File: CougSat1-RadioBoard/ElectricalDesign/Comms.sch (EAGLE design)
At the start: 409 parts, among them J1 230mm Antenna, J2 CougSat Card, J3 700mm Antenna, J4 SWD, Q1 CSD25402Q3A, Q12 DMN53D0LDW, Q2 CSD25402Q3A, Q3 DMN53D0LDW, Q9 DMN53D0LDW, U1 INA199C1, U10 HMC452QS16G, U11 AD8515, U12 AD7291, U13 AD8515, U14 LP5907MFX-3.1, U15 AD9761, U16 TXS0102DQM, U18 TXS0102DQM, U19 MMZ09332B, U2 LP5907MFX-3.1, U20 ADF4360, U21 HMC545A, U22 AD9761, U23 MAAM-011229, U24 AD8515, U25 MAAM-011229, U26 AD8345, U28 AD8348, U29 AD7291, U3 TPS61236, U30 TXS0102DQM, U31 MAAM-011229, U32 AD8515, U35 TXS0102DQM, U36 ADF4360, U37 MAAM-011229, U39 AD8515, U4 AD8346, U40 AD8515, U42 TXS0102DQM, U43 INA199C2, U44 TXS0102DQM, U45 TXS0102DQM, U46 TXS0102DQM, U47 TXS0102DQM, U48 AD7291, U49 AD8515, U5 ADF4360, U50 INA199C2, U51 LP5907MFX-3.1, U52 INA199C2, U53 INA199C1, U54 TXS0102DQM, U55 TXS0102DQM, U6 STM32L496VGT, U7 GRF2133, U8 IS25LP016D, U9 IS25LP016D, Y1 19.68MHz ±2.5ppm, Y2 8MHz ±10ppm, Y3 32.768kHz ±10ppm, Y4 19.68MHz ±2.5ppm, Y5 19.68MHz ±2.5ppm

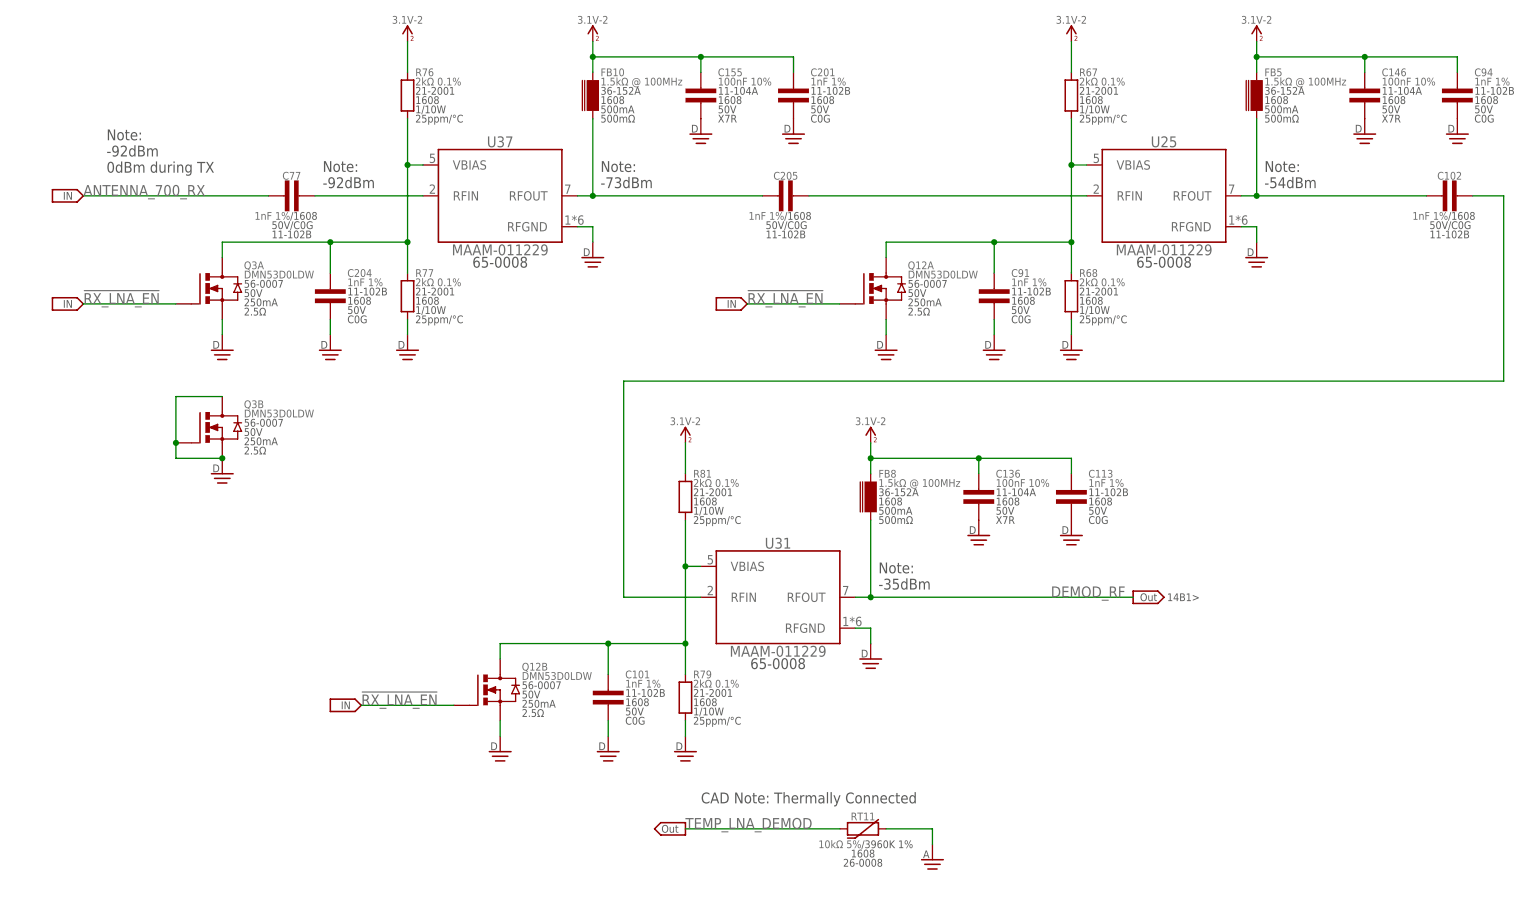
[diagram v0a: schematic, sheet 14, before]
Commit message: Laid out 700mm demodulator
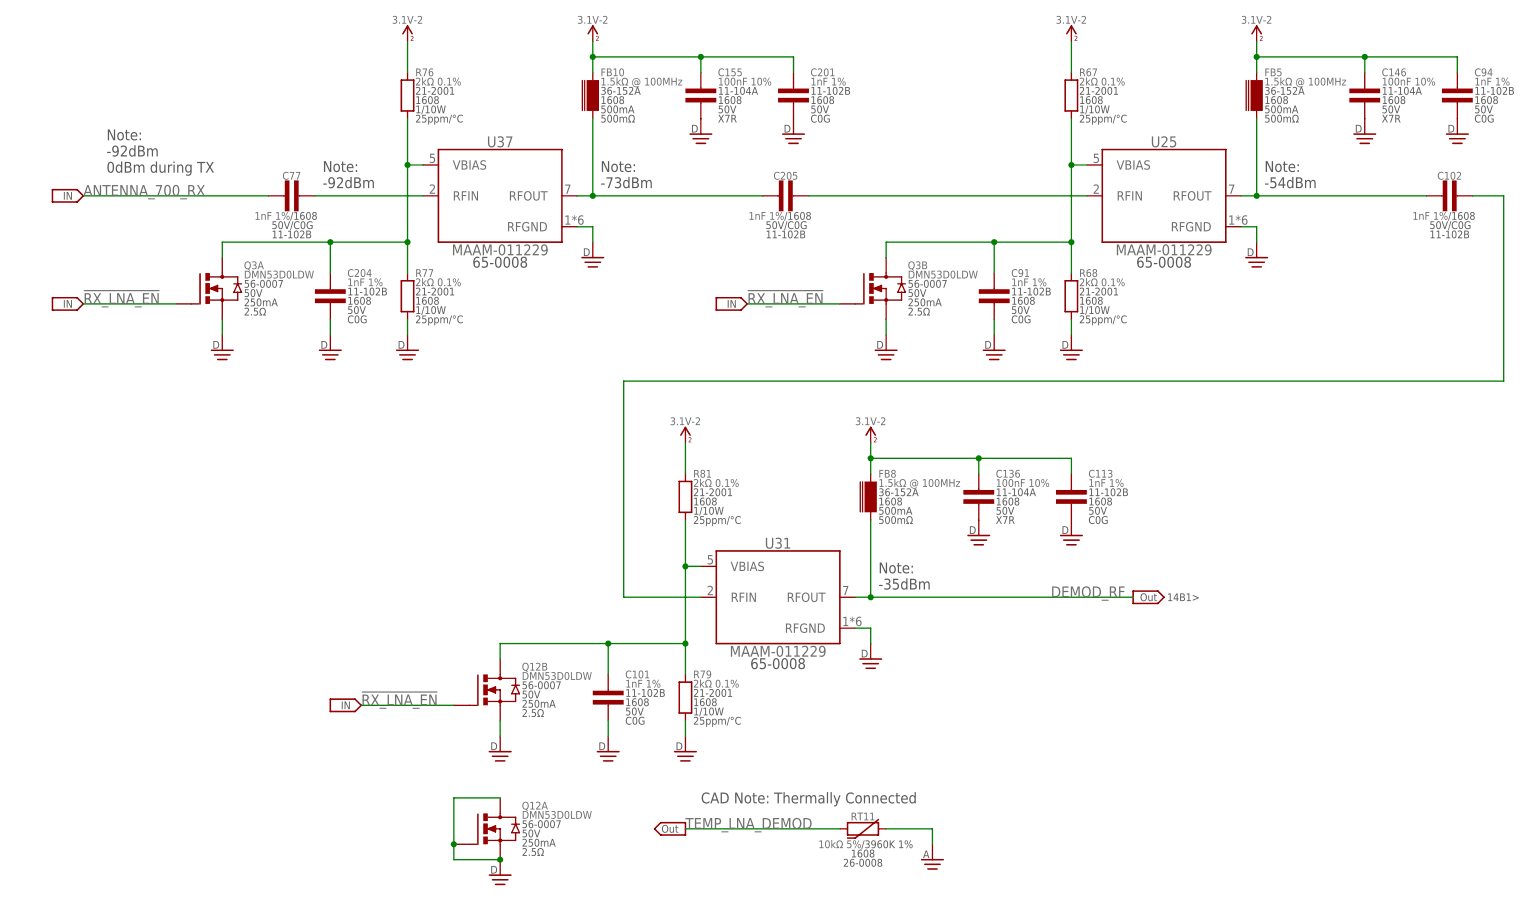
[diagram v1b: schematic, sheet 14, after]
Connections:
- net !RX_LNA_EN: now also Q3B.G; no longer Q12A.G
- net DGND: now also Q12A.D, Q12A.G; no longer Q3B.D, Q3B.G
- net RX_LNA_BIAS-1: now also Q3B.D; no longer Q12A.D
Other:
- moved on the sheet: Q12A, Q3B
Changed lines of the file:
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@@
 <attribute name="SKU" x="179.07" y="123.952" size="1.27" layer="97" align="center-left"/>
-</instance>
-<instance part="Q12" gate="A" x="147.32" y="124.46" smashed="yes">
-<attribute name="NAME" x="150.876" y="128.27" size="1.27" layer="95" align="center-left"/>
-<attribute name="VALUE" x="150.876" y="126.746" size="1.27" layer="96" align="center-left"/>
-<attribute name="SKU" x="150.876" y="125.222" size="1.27" layer="97" align="center-left"/>
-<attribute name="VDS" x="150.876" y="123.698" size="1.27" layer="97" align="center-left"/>
-<attribute name="CURRENT" x="150.876" y="122.174" size="1.27" layer="97" align="center-left"/>
-<attribute name="RDS" x="150.876" y="120.65" size="1.27" layer="97" align="center-left"/>
 </instance>
 <instance part="OFFSHEET78" gate="G$1" x="121.92" y="121.92" smashed="yes"/>
@@
 <instance part="SUPPLY371" gate="G$1" x="99.06" y="165.1" smashed="yes">
 <attribute name="VALUE" x="99.06" y="168.656" size="1.27" layer="96" align="center"/>
-</instance>
-<instance part="Q3" gate="B" x="38.1" y="101.6" smashed="yes">
-<attribute name="NAME" x="41.656" y="105.41" size="1.27" layer="95" align="center-left"/>
-<attribute name="VALUE" x="41.656" y="103.886" size="1.27" layer="96" align="center-left"/>
-<attribute name="SKU" x="41.656" y="102.362" size="1.27" layer="97" align="center-left"/>
-<attribute name="VDS" x="41.656" y="100.838" size="1.27" layer="97" align="center-left"/>
-<attribute name="CURRENT" x="41.656" y="99.314" size="1.27" layer="97" align="center-left"/>
-<attribute name="RDS" x="41.656" y="97.79" size="1.27" layer="97" align="center-left"/>
 </instance>
 <instance part="SUPPLY197" gate="1" x="83.82" y="48.26" smashed="yes"/>
@@
 <instance part="SUPPLY293" gate="1" x="68.58" y="114.3" smashed="yes"/>
 <instance part="SUPPLY294" gate="1" x="55.88" y="114.3" smashed="yes"/>
-<instance part="SUPPLY295" gate="1" x="38.1" y="93.98" smashed="yes"/>
+<instance part="SUPPLY295" gate="1" x="83.82" y="27.94" smashed="yes"/>
 <instance part="SUPPLY296" gate="1" x="38.1" y="114.3" smashed="yes"/>
+<instance part="Q3" gate="B" x="147.32" y="124.46" smashed="yes">
+<attribute name="NAME" x="150.876" y="128.27" size="1.27" layer="95" align="center-left"/>
+<attribute name="VALUE" x="150.876" y="126.746" size="1.27" layer="96" align="center-left"/>
+<attribute name="SKU" x="150.876" y="125.222" size="1.27" layer="97" align="center-left"/>
+<attribute name="VDS" x="150.876" y="123.698" size="1.27" layer="97" align="center-left"/>
+<attribute name="CURRENT" x="150.876" y="122.174" size="1.27" layer="97" align="center-left"/>
+<attribute name="RDS" x="150.876" y="120.65" size="1.27" layer="97" align="center-left"/>
+</instance>
+<instance part="Q12" gate="A" x="83.82" y="35.56" smashed="yes">
+<attribute name="NAME" x="87.376" y="39.37" size="1.27" layer="95" align="center-left"/>
+<attribute name="VALUE" x="87.376" y="37.846" size="1.27" layer="96" align="center-left"/>
+<attribute name="SKU" x="87.376" y="36.322" size="1.27" layer="97" align="center-left"/>
+<attribute name="VDS" x="87.376" y="34.798" size="1.27" layer="97" align="center-left"/>
+<attribute name="CURRENT" x="87.376" y="33.274" size="1.27" layer="97" align="center-left"/>
+<attribute name="RDS" x="87.376" y="31.75" size="1.27" layer="97" align="center-left"/>
+</instance>
 </instances>
 <busses>
@@
 <net name="!RX_LNA_EN" class="0">
 <segment>
-<pinref part="Q12" gate="A" pin="G"/>
 <wire x1="139.7" y1="121.92" x2="124.46" y2="121.92" width="0.1524" layer="91"/>
 <label x="124.46" y="121.92" size="1.778" layer="95"/>
+<pinref part="Q3" gate="B" pin="G"/>
 </segment>
 <segment>
@@
 <wire x1="177.8" y1="144.78" x2="180.34" y2="144.78" width="0.1524" layer="91"/>
 <junction x="177.8" y="144.78"/>
-<pinref part="Q12" gate="A" pin="D"/>
 <wire x1="165.1" y1="132.08" x2="147.32" y2="132.08" width="0.1524" layer="91"/>
 <wire x1="147.32" y1="132.08" x2="147.32" y2="129.54" width="0.1524" layer="91"/>
 <junction x="165.1" y="132.08"/>
+<pinref part="Q3" gate="B" pin="D"/>
 </segment>
 </net>
@@
 </segment>
 <segment>
-<pinref part="Q12" gate="A" pin="S"/>
 <wire x1="147.32" y1="119.38" x2="147.32" y2="116.84" width="0.1524" layer="91"/>
 <pinref part="SUPPLY275" gate="1" pin="DGND"/>
+<pinref part="Q3" gate="B" pin="S"/>
 </segment>
 <segment>
@@
 </segment>
 <segment>
-<wire x1="38.1" y1="106.68" x2="30.48" y2="106.68" width="0.1524" layer="91"/>
-<wire x1="30.48" y1="106.68" x2="30.48" y2="99.06" width="0.1524" layer="91"/>
-<wire x1="30.48" y1="99.06" x2="30.48" y2="96.52" width="0.1524" layer="91"/>
-<wire x1="30.48" y1="96.52" x2="38.1" y2="96.52" width="0.1524" layer="91"/>
-<pinref part="Q3" gate="B" pin="G"/>
-<junction x="30.48" y="99.06"/>
-<pinref part="Q3" gate="B" pin="D"/>
-<pinref part="Q3" gate="B" pin="S"/>
+<wire x1="83.82" y1="40.64" x2="76.2" y2="40.64" width="0.1524" layer="91"/>
+<wire x1="76.2" y1="40.64" x2="76.2" y2="33.02" width="0.1524" layer="91"/>
+<wire x1="76.2" y1="33.02" x2="76.2" y2="30.48" width="0.1524" layer="91"/>
+<wire x1="76.2" y1="30.48" x2="83.82" y2="30.48" width="0.1524" layer="91"/>
 <pinref part="SUPPLY295" gate="1" pin="DGND"/>
-<junction x="38.1" y="96.52"/>
-</segment>
-<segment>
+<pinref part="Q12" gate="A" pin="G"/>
+<junction x="76.2" y="33.02"/>
+<pinref part="Q12" gate="A" pin="D"/>
+<pinref part="Q12" gate="A" pin="S"/>
+<junction x="83.82" y="30.48"/>
+</segment>
+<segment>

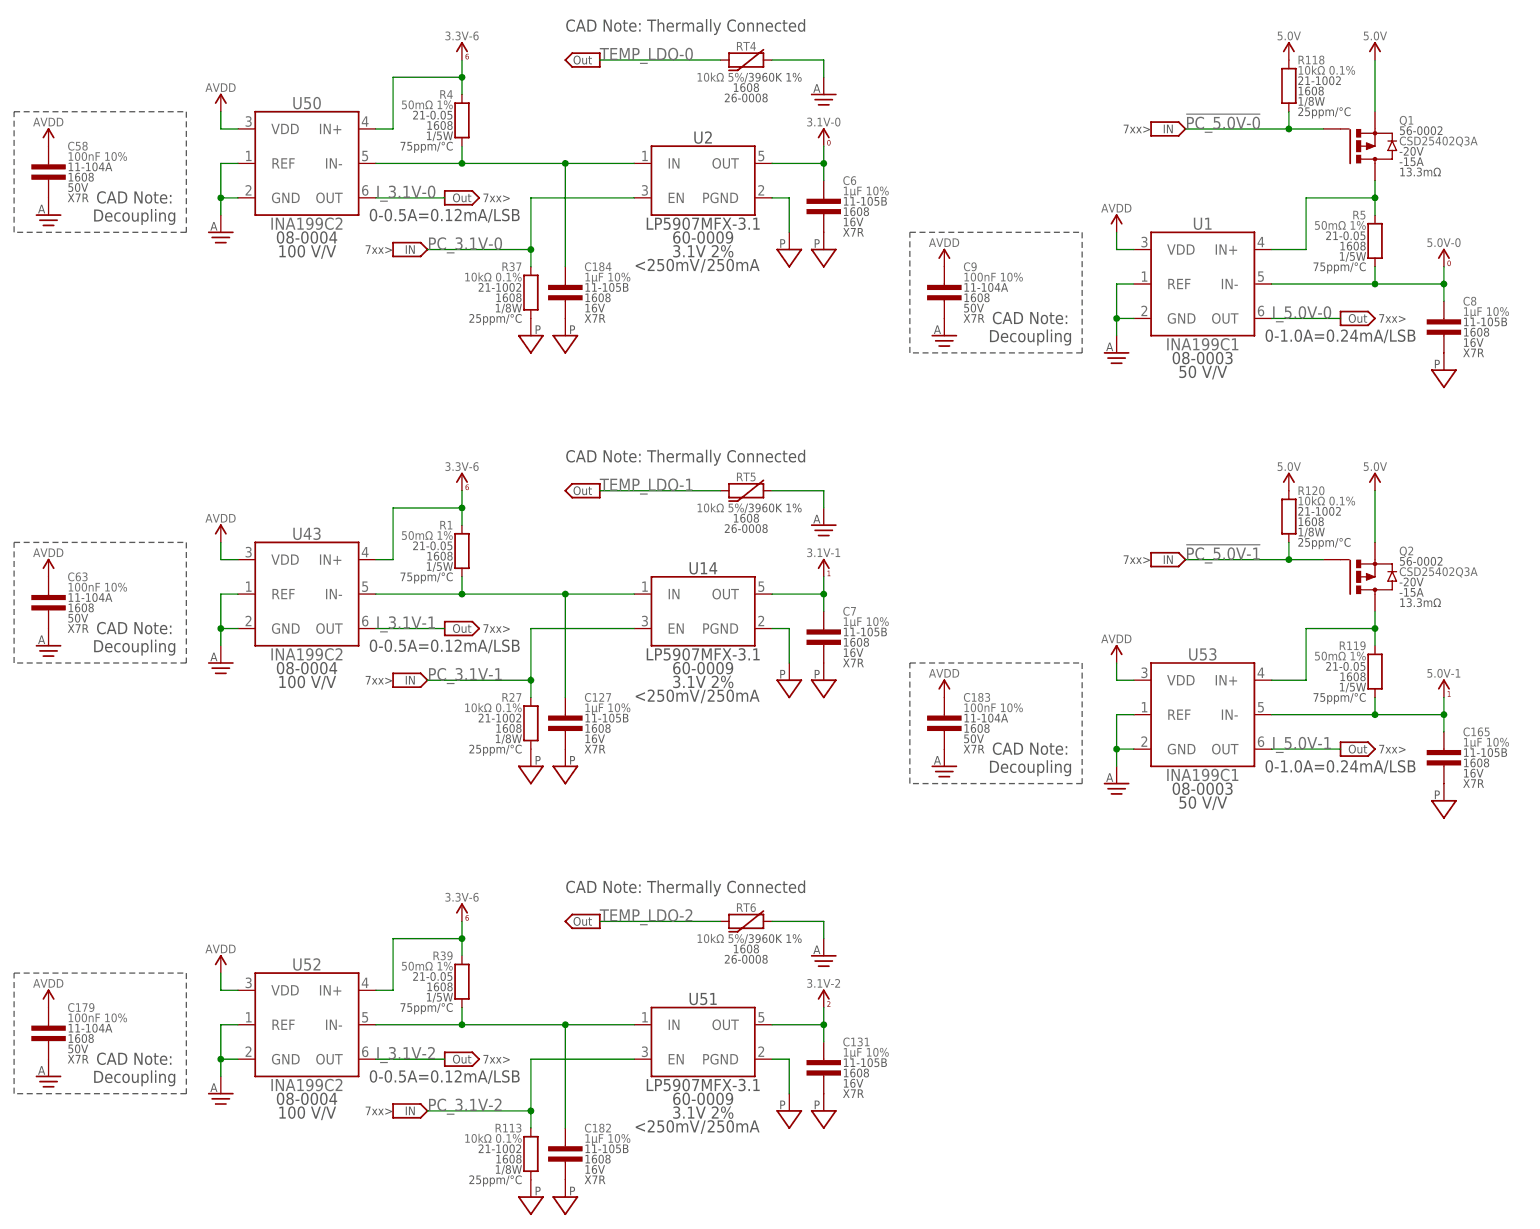
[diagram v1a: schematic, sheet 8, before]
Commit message: Laid out SPI flash and ADCs :rocket:
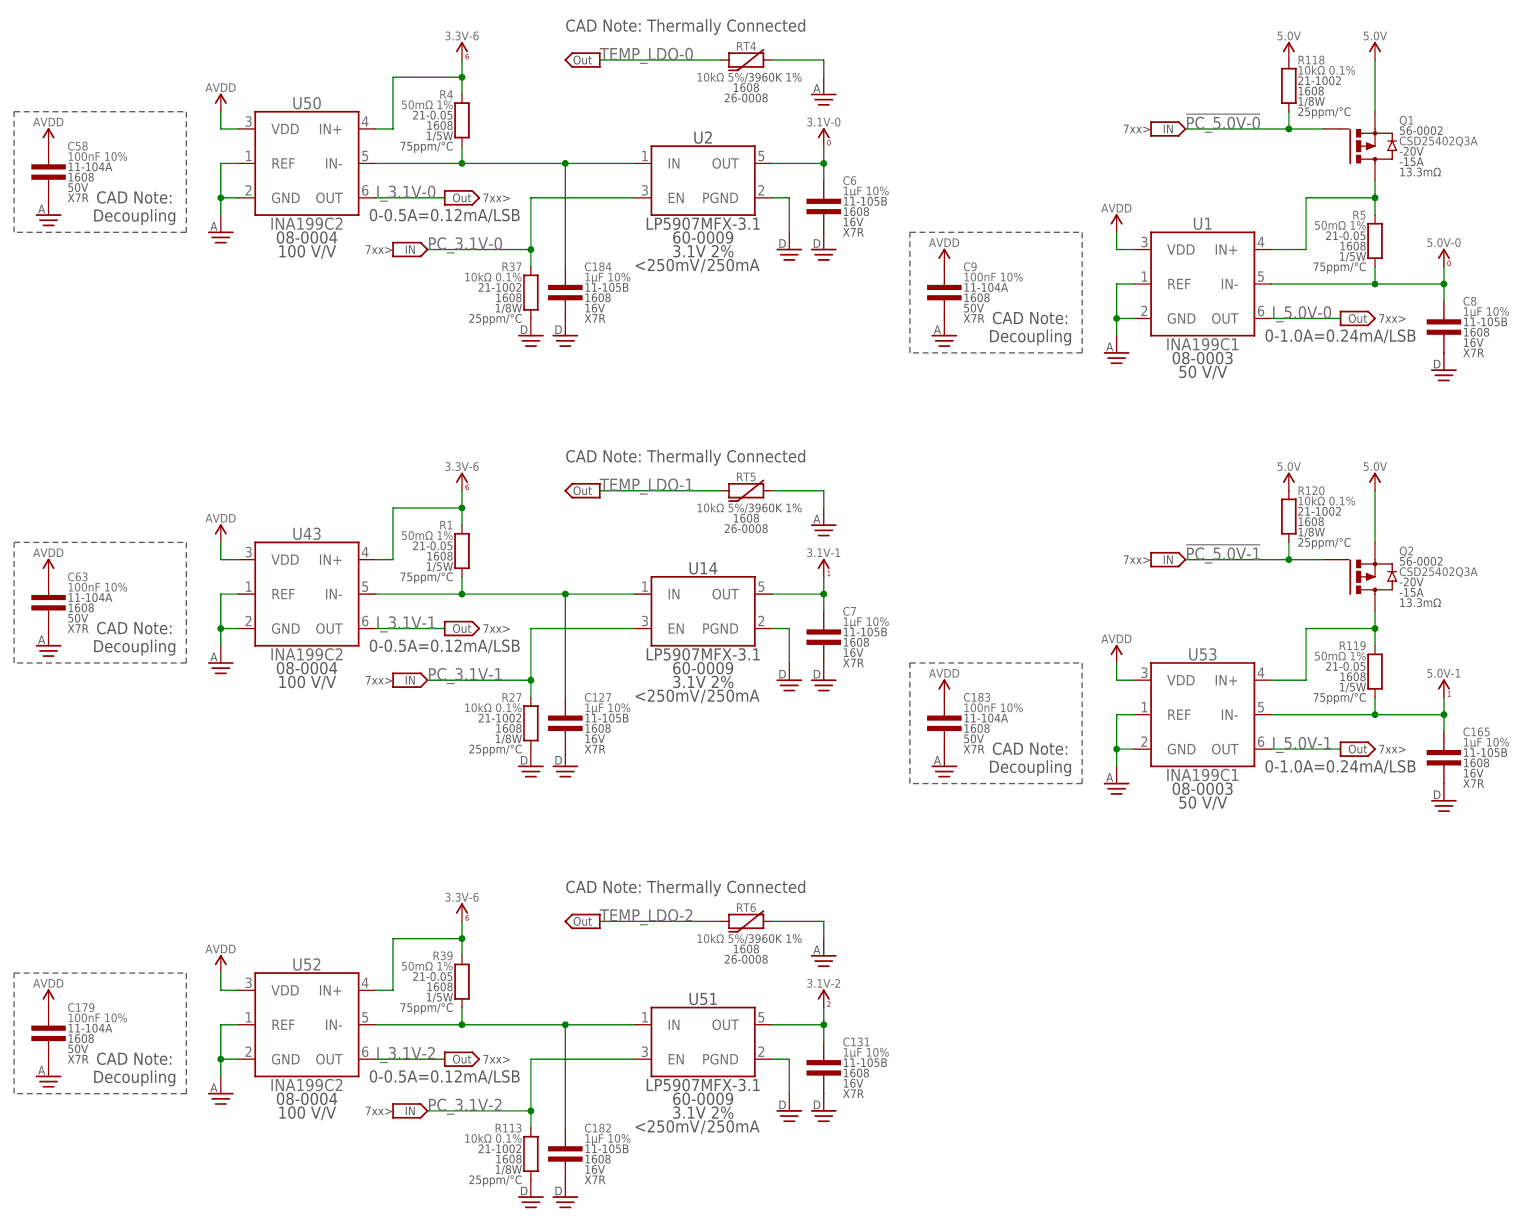
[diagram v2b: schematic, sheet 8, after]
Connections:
- net !FLASH_CS-A: now also U6B.PB5
- net !FLASH_CS-B: now also U6B.PB8
- net !FLASH_WP: now also U6B.PB9
- net DAC_BUS_CLK-230: now also U6E.PE5; no longer U6E.PE3
- net DAC_SELECT_I/!Q: now also U6E.PE3; no longer U6E.PE5
- net DGND: now also C127.2, C131.2, C165.2, C182.2, C184.2, C6.2, C7.2, C8.2, R113.1, R27.1, R37.1, U14.PGND, U2.PGND, U51.PGND
- net PGND: no longer C127.2, C131.2, C165.2, C182.2, C184.2, C6.2, C7.2, C8.2, R113.1, R27.1, R37.1, U14.PGND, U2.PGND, U51.PGND
